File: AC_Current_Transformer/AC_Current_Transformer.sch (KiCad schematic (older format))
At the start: 6 parts, among them J101 Interface, J102 AudioJack3

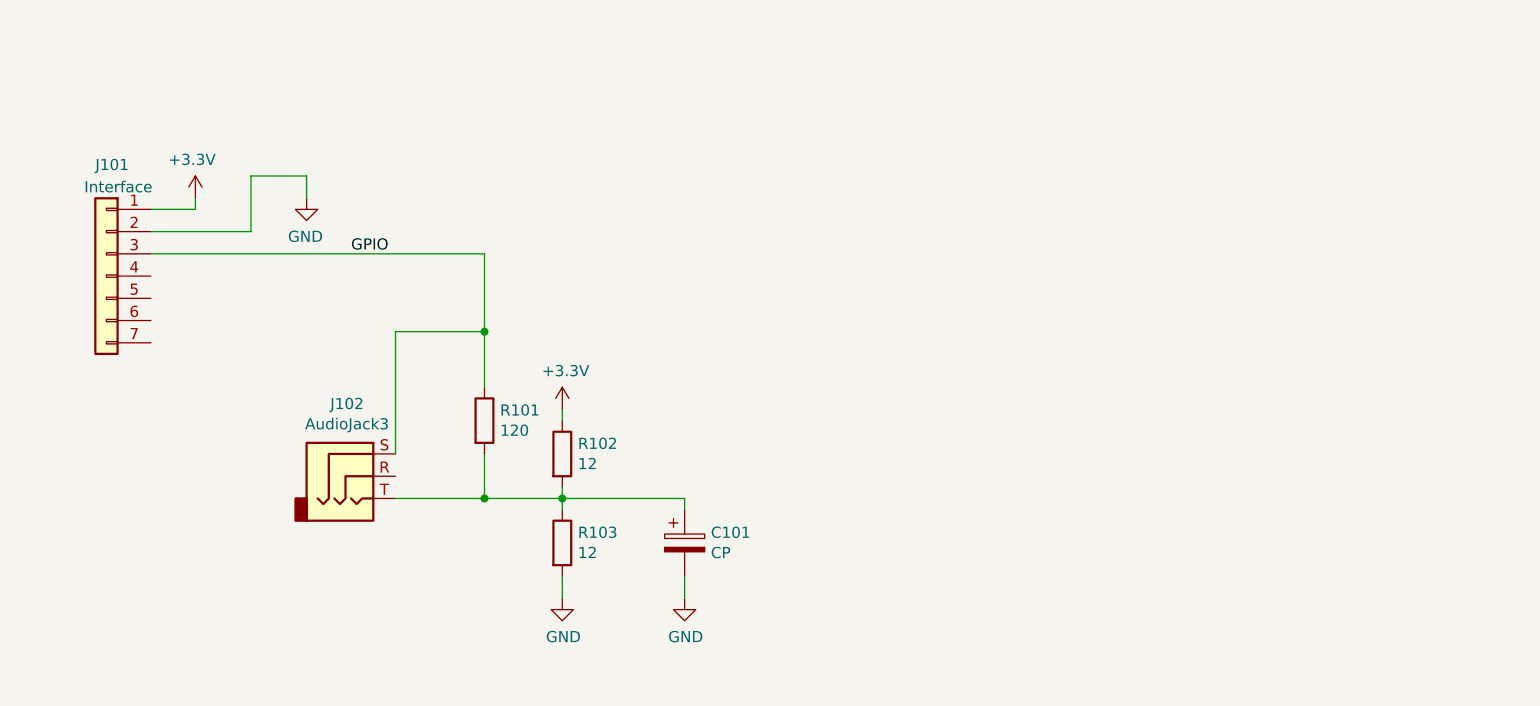
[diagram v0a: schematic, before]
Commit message: New GND Pin.  Added PI Filters to all inputs.    Refined Layout
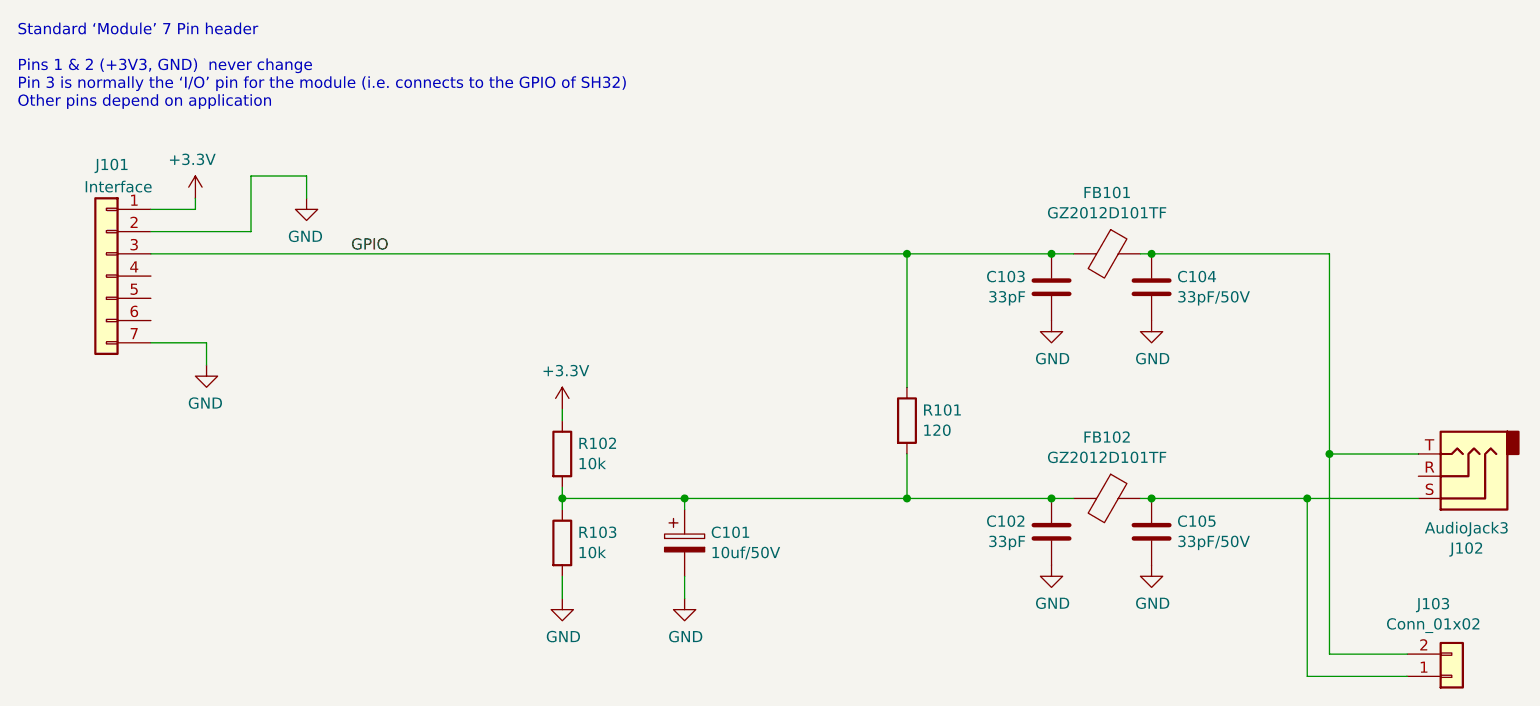
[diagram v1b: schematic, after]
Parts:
- added C102, C103: 33pF, Capacitor_SMD:C_0402_1005Metric, symbol Device:C
- added C104, C105: 33pF/50V, Capacitor_SMD:C_0603_1608Metric, symbol Device:C
- added FB101, FB102: GZ2012D101TF, Inductor_SMD:L_0805_2012Metric, symbol Device:Ferrite_Bead
- added J103: Conn_01x02, Connector_PinHeader_2.54mm:PinHeader_1x02_P2.54mm_Horizontal, symbol Connector_Generic:Conn_01x02
- C101: value CP -> 10uf/50V; footprint Capacitor_SMD:C_0603_1608Metric -> Capacitor_SMD:C_1206_3216Metric; LCSC (none) -> C13585
- R102, R103: value 12 -> 10k
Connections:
- net GND: now also J101.7 (Pin_7), C102.2, C103.2, C104.2, C105.2
- net GPIO: now also C103.1, FB101.2; no longer J102.S
- net at C101.1, R101.2, R102.2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: now also C102.1, FB102.2; no longer J102.T
- new net: C104.1, FB101.1, J102.T, J103.2 (Pin_2)
- new net: C105.1, FB102.1, J102.S, J103.1 (Pin_1)
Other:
- note added: "Standard ‘Module’ 7 Pin header\n\nPins 1 & 2 (+3V3, GND) never change\nPin 3 is normally the ‘I/O’ pin for the module (i.e. connects to the GPIO of SH32)\nOther pins depend on application"
- moved on the sheet: J102, R101
